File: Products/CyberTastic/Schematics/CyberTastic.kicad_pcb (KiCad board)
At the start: 2 copper layers, 52 parts, among them J1 USB_C_Receptacle, J2 U.FL, J3 USB_C_Receptacle, J4 Conn_01x04, J5 Conn_01x07, J6 Conn_01x01, J7 Conn_01x01, J8 OledDisplay, J9 Conn_01x04, Q1 AO3401A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

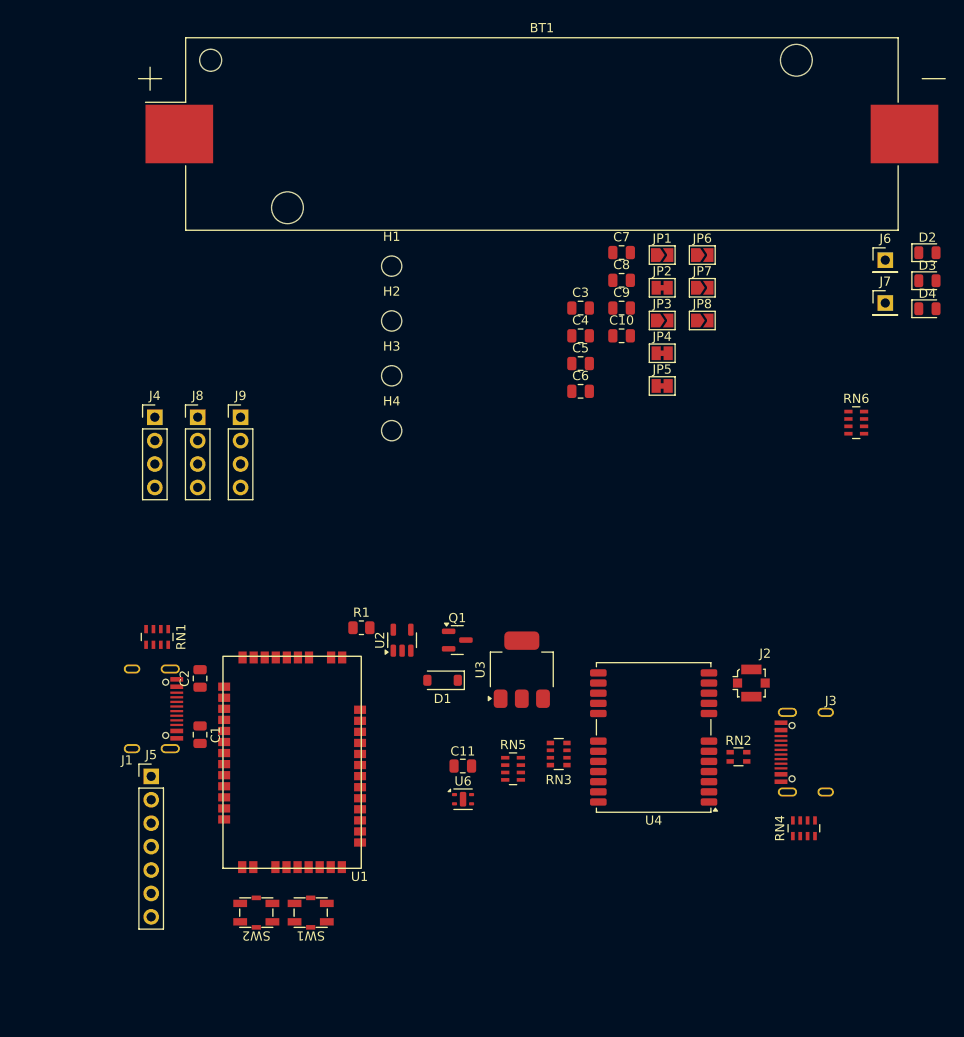
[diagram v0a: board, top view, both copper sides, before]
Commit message: Completed V1 Routing
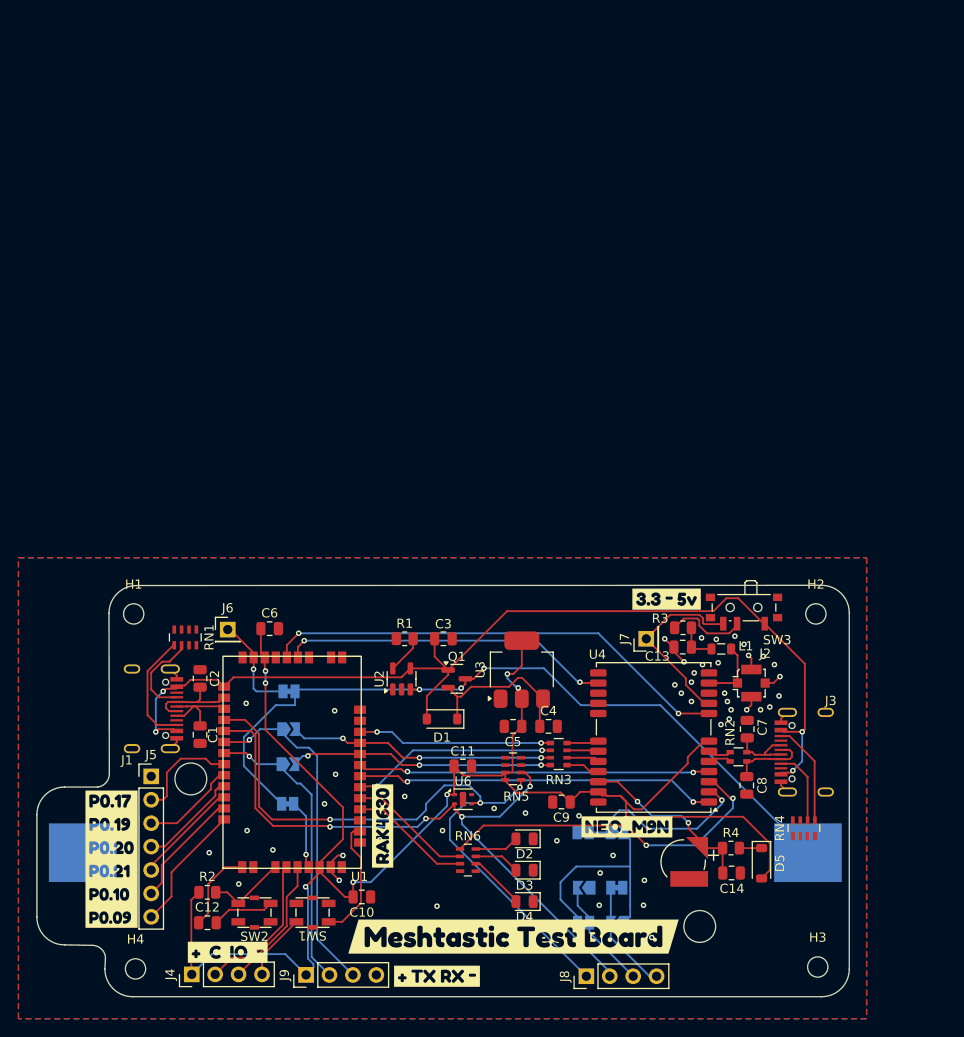
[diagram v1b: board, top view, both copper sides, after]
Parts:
- added BT2: Battery_Cell, UE-Battery:SEIKO_ML414H_IV01E, F.Cu at (175.1, 146.0)
- added C12: 100nF, Capacitor_SMD:C_0805_2012Metric, F.Cu at (123.5, 152.6)
- added C13: 100nF, Capacitor_SMD:C_0805_2012Metric, F.Cu at (175.1, 122.7)
- added C14: 100nF, Capacitor_SMD:C_0805_2012Metric, F.Cu at (180.3, 147.2)
- added D5: D_Schottky, Diode_SMD:D_SOD-123, F.Cu at (183.6, 146.1)
- added JP10: Jumper_2_Bridged, Jumper:SolderJumper-2_P1.3mm_Bridged_Pad1.0x1.5mm, B.Cu at (132.2, 139.7)
- added JP9: Jumper_2_Bridged, Jumper:SolderJumper-2_P1.3mm_Bridged_Pad1.0x1.5mm, B.Cu at (132.3, 127.5)
- added L1: 27nH, Inductor_SMD:L_0805_2012Metric, F.Cu at (179.2, 122.9)
- added R2: 10k, Resistor_SMD:R_0805_2012Metric, F.Cu at (123.5, 149.3)
- added R3: 10, Resistor_SMD:R_0805_2012Metric, F.Cu at (175.1, 120.6)
- added R4: 1k, Resistor_SMD:R_0805_2012Metric, F.Cu at (180.3, 144.5)
- added SW3: SW_SPDT, Button_Switch_SMD:SW_SPDT_PCM12, F.Cu at (181.7, 118.7)
- added kibuzzard-665A1BDF: G***, kibuzzard-665A1BDF, F.Cu at (156.7, 154.1)
- added kibuzzard-665A1C19: G***, kibuzzard-665A1C19, F.Cu at (113.1, 145.7)
- added kibuzzard-665A1C85: G***, kibuzzard-665A1C85, F.Cu at (125.7, 155.8)
- added kibuzzard-665A1CA2: G***, kibuzzard-665A1CA2, F.Cu at (148.4, 158.4)
- added kibuzzard-665A1CD2: G***, kibuzzard-665A1CD2, F.Cu at (173.3, 117.5)
- added kibuzzard-665A1D5A: G***, kibuzzard-665A1D5A, F.Cu at (142.5, 142.1)
- added kibuzzard-665A1D6B: G***, kibuzzard-665A1D6B, F.Cu at (169.0, 142.2)
- BT1, JP1, JP2, JP3, JP4, JP5, JP6, JP7, JP8: moved to B.Cu
- J6: value Conn_01x01 -> Bodge
- moved J6 81.8 mm to (125.7, 120.8)
- moved H3 79.0 mm to (189.7, 157.4)
- moved BT1 78.7 mm to (149.3, 145.0), turned to 180 degrees
- moved D4 77.7 mm to (157.9, 150.3), turned to 180 degrees
- moved D3 77.4 mm to (157.9, 146.9), turned to 180 degrees
- moved D2 77.1 mm to (157.9, 143.5), turned to 180 degrees
- moved J8 73.8 mm to (164.6, 158.4), turned to 90 degrees
- moved JP1 72.6 mm to (168.0, 152.6), turned to 180 degrees
- moved C10 67.1 mm to (140.2, 149.8), turned to 180 degrees
- moved JP8 65.9 mm to (132.2, 135.4)
- moved JP7 65.6 mm to (132.3, 131.6)
- moved JP2 65.3 mm to (167.9, 148.8), turned to 180 degrees
- moved H4 64.7 mm to (115.7, 157.6)
- moved RN6 63.4 mm to (151.8, 145.8)
- moved JP6 63.3 mm to (167.9, 142.8)
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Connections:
- J5 pad 1: P0.16 -> VSS
- J9 pad 2: RX -> TX
- J9 pad 3: TX -> RX
- RN1 pad 3: unconnected-(RN1-R3.1-Pad3) -> VSS
- RN1 pad 4: unconnected-(RN1-R4.1-Pad4) -> VSS
- RN3 pad 5: /SCL/CLK -> /SDA/CS
- RN3 pad 6: /SDA/CS -> /SCL/CLK
- RN3 pad 7: /RX/MOSI -> /TX/MISO
- RN3 pad 8: /TX/MISO -> /RX/MOSI
- RN4 pad 3: unconnected-(RN4-R3.1-Pad3) -> VSS
- RN4 pad 4: unconnected-(RN4-R4.1-Pad4) -> VSS
- RN6 pad 2: LED1 -> LED2
- RN6 pad 3: LED2 -> LED1
- SW2 pad 2: VSS -> Net-(SW2-B)
- U1 pad 20: VCC -> Net-(JP10-B)
- U4 pad 18: Net-(RN3-R3.1) -> Net-(RN3-R4.1)
- U4 pad 19: Net-(RN3-R4.1) -> Net-(RN3-R3.1)
- U4 pad 20: Net-(RN3-R1.1) -> Net-(RN3-R2.1)
- U4 pad 21: Net-(RN3-R2.1) -> Net-(RN3-R1.1)
- U4 pad 22: Batt -> Net-(BT2-+)
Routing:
- net VCC: track 0.00 -> 194.4 mm, vias 0 -> 8
- net +5V: track 0.00 -> 111.1 mm, vias 0 -> 4
- net Batt: track 0.00 -> 83.7 mm, vias 0 -> 3
- net SDA: track 0.00 -> 74.1 mm, vias 0 -> 3
- net SCL: track 0.00 -> 71.6 mm, vias 0 -> 4
- net RESET: track 0.00 -> 51.3 mm, vias 0 -> 2
- net SAFEBOOT: track 0.00 -> 39.1 mm, vias 0 -> 2
- net EXTINT: track 0.00 -> 38.2 mm, vias 0 -> 2
- net Timepulse: track 0.00 -> 37.6 mm, vias 0 -> 2
- net RX: track 0.00 -> 37.5 mm, vias 0 -> 1
- net LND_EN: track 0.00 -> 35.9 mm, vias 0 -> 2
- net VSS: track 0.00 -> 35.3 mm, vias 0 -> 51
- net TX: track 0.00 -> 31.9 mm, vias 0 -> 1
- net /TX/MISO: track 0.00 -> 29.0 mm, vias 0 -> 3
- net /RX/MOSI: track 0.00 -> 28.7 mm, vias 0 -> 3
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- added copper zone on B.Cu, net VSS
- added copper zone on F.Cu, net VSS
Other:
- board outline added: 88.1 x 44.6 mm

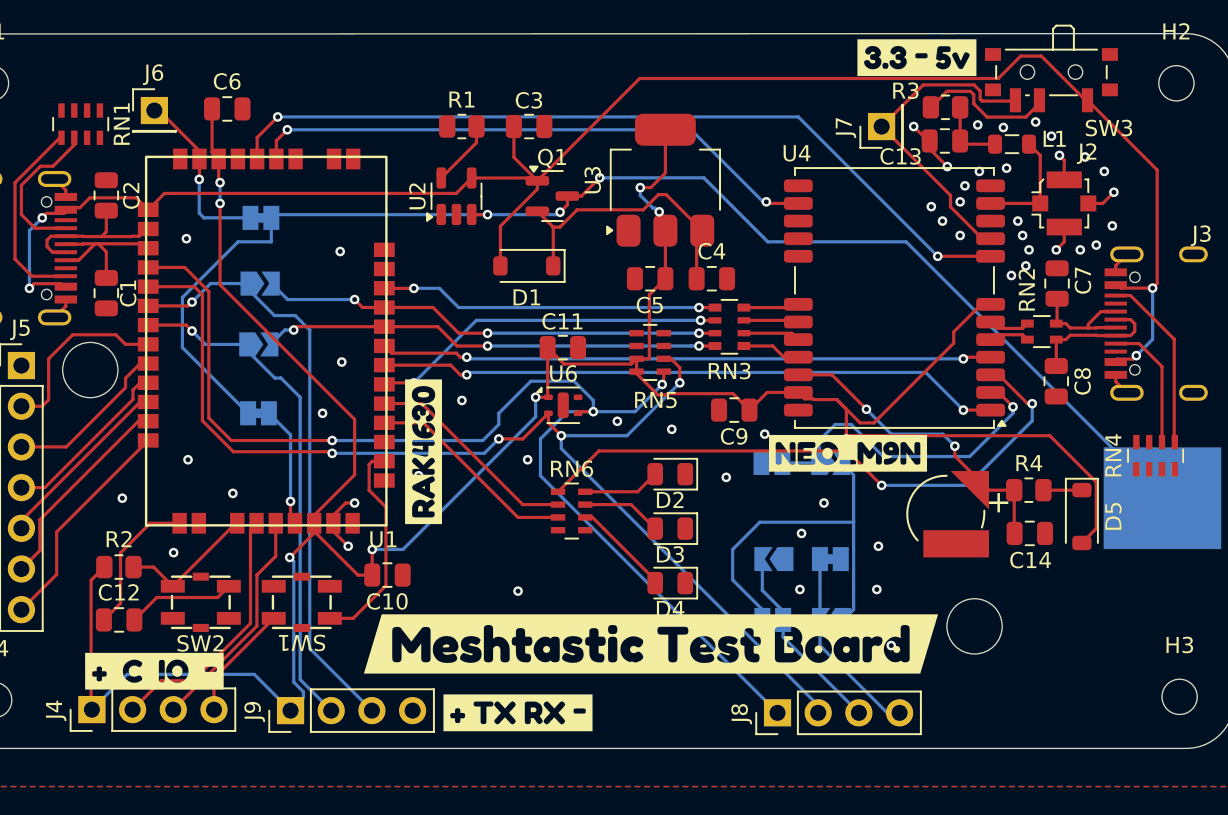
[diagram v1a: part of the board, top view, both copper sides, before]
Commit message: Moved gaussmouse and ordered V1
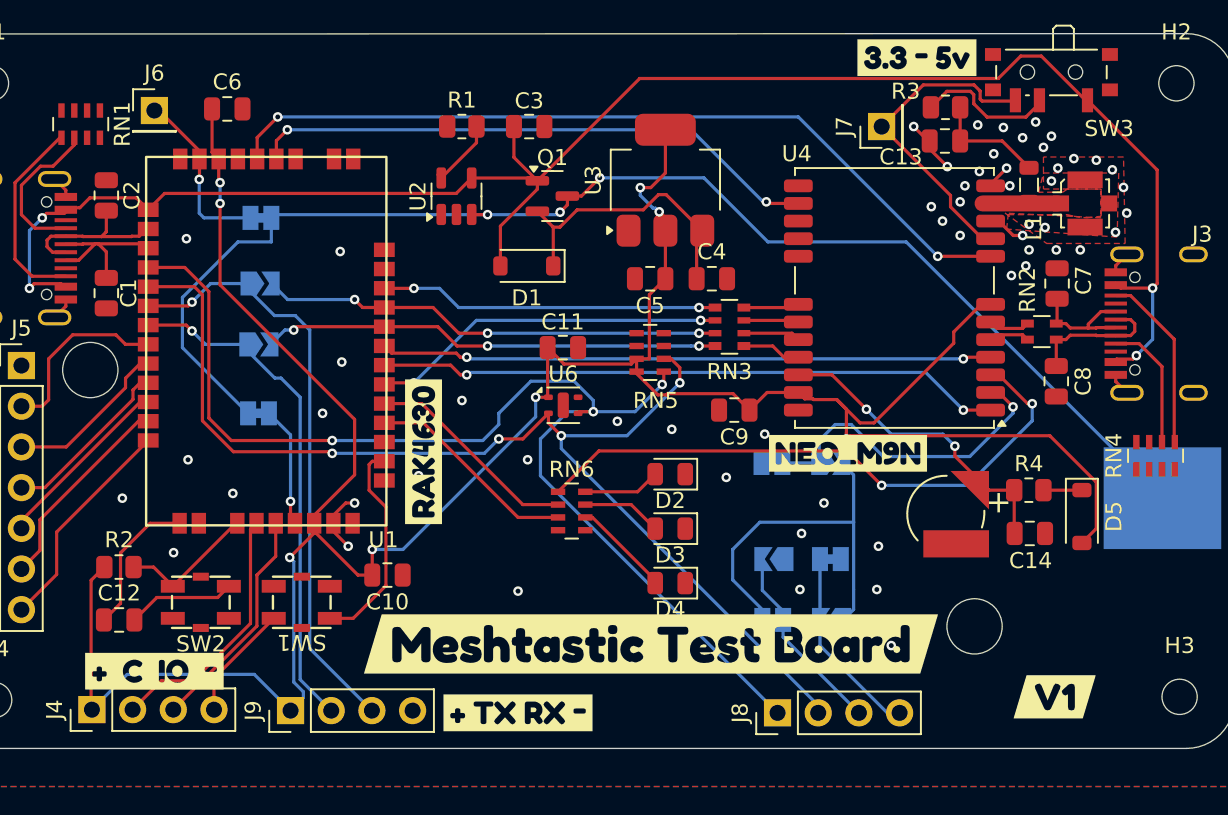
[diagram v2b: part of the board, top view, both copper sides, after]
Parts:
- added kibuzzard-665A1E07: G***, kibuzzard-665A1E07, F.Cu at (181.9, 157.4)
- moved L1 2.75 mm to (180.3, 125.4), turned to 90 degrees
- moved J2 1.30 mm to (183.8, 126.6)
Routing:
- net Net-(C13-Pad1): track 4.36 -> 7.38 mm
- net VSS: track 35.3 -> 34.0 mm, vias 51 -> 58
- net Net-(J2-In): track 7.09 -> 6.22 mm
